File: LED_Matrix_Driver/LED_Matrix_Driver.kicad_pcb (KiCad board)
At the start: 4 copper layers, 76 parts, among them J1 Audio In, J2 Screw_Terminal_01x02, J3 Buttons, J4 LED Anode Rows, J5 Columns 24-31 LED Cathodes, J6 Columns 16-23 LED Cathodes, J7 Columns 8-15 LED Cathodes, J8 Columns 0-7 LED Cathodes, U1 ESP32-DEVKITC-32E, U2 74HCT244, U3 MIC2981, U4 74HC238, U5 HEF4794B, U6 HEF4794B, U7 HEF4794B, U8 HEF4794B

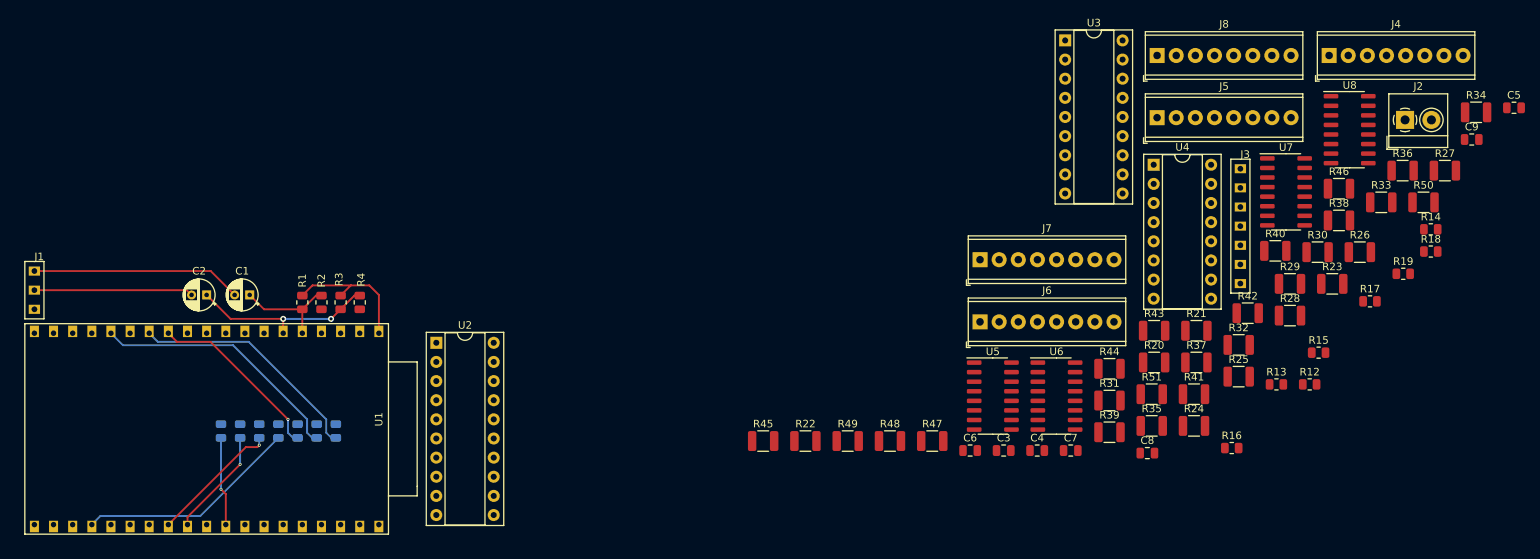
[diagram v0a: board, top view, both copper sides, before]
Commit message: Finished PCB design for board revision 1.1
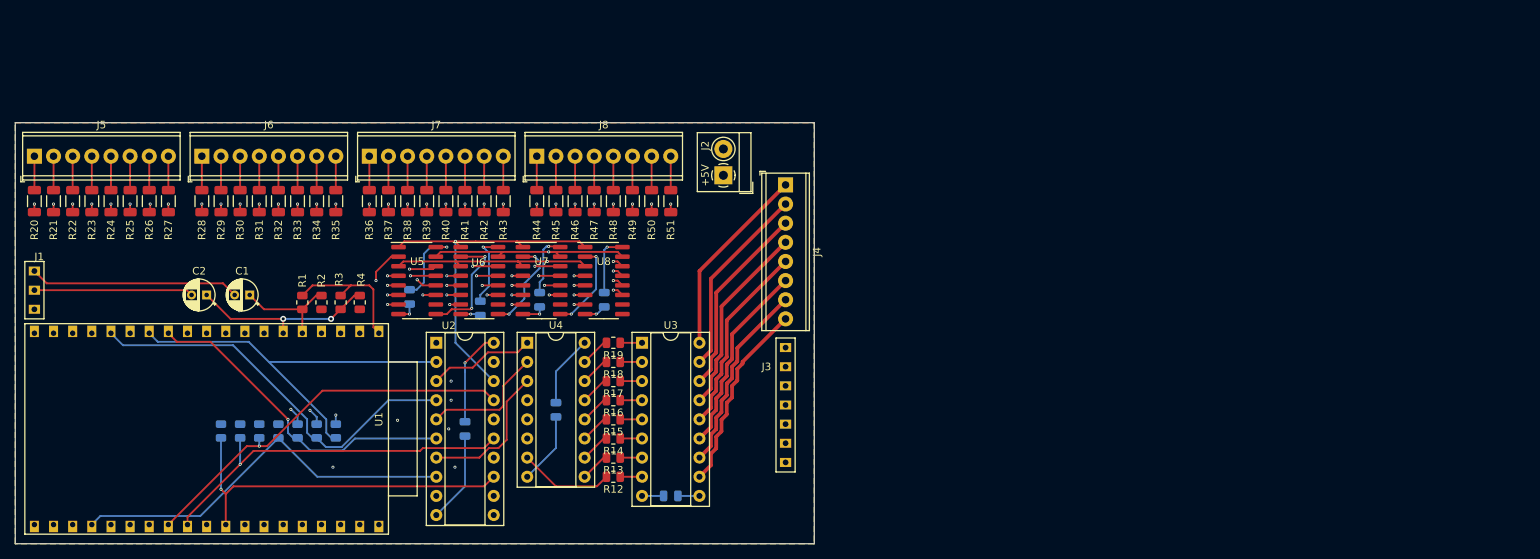
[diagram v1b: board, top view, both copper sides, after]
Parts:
- C3, C4, C5, C6, C7, C8, C9: moved to B.Cu
- R20, R21, R22, R23, R24, R25, R26, R27, R28, R29, R30, R31, R32, R33, R34, R35, R36, R37, R38, R39, R40, R41, R42, R43, R44, R45, R46, R47, R48, R49, R50, R51: footprint Resistor_SMD:R_1210_3225Metric -> Resistor_SMD:R_1206_3216Metric
- moved R27 169.5 mm to (32.4, 91.7), turned to 270 degrees
- moved R23 165.0 mm to (22.2, 91.7), turned to 270 degrees
- moved R26 160.8 mm to (29.8, 91.7), turned to 270 degrees
- moved R34 154.3 mm to (52.1, 91.7), turned to 270 degrees
- moved R21 152.7 mm to (17.1, 91.7), turned to 270 degrees
- moved R20 150.1 mm to (14.6, 91.7), turned to 270 degrees
- moved J5 149.1 mm to (14.6, 85.7)
- moved R25 149.0 mm to (27.3, 91.7), turned to 270 degrees
- moved R24 146.8 mm to (24.8, 91.7), turned to 270 degrees
- moved R28 145.2 mm to (36.8, 91.7), turned to 270 degrees
- moved R33 143.8 mm to (49.5, 91.7), turned to 270 degrees
- moved R30 143.2 mm to (41.9, 91.7), turned to 270 degrees
- moved R29 142.3 mm to (39.4, 91.7), turned to 270 degrees
- moved R36 137.2 mm to (59.1, 91.7), turned to 270 degrees
- moved C5 133.3 mm to (83.8, 119.4), turned to 270 degrees
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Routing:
- net Net-(J3-Pad6): track 0.00 -> 93.6 mm
- net Net-(J3-Pad5): track 0.00 -> 92.7 mm
- net Net-(J3-Pad1): track 0.00 -> 91.7 mm
- net Net-(J3-Pad2): track 0.00 -> 84.4 mm
- net Net-(J3-Pad3): track 0.00 -> 74.6 mm
- net Net-(J3-Pad4): track 0.00 -> 69.9 mm
- net Net-(U2-Pad12): track 0.00 -> 66.5 mm, vias 0 -> 1
- net +5V: track 0.00 -> 62.8 mm, vias 0 -> 5
- net Net-(U2-Pad14): track 0.00 -> 58.8 mm, vias 0 -> 1
- net Net-(R22-Pad2): track 0.00 -> 54.2 mm, vias 0 -> 2
- net Net-(R20-Pad2): track 0.00 -> 53.2 mm, vias 0 -> 2
- net Net-(R23-Pad2): track 0.00 -> 53.0 mm, vias 0 -> 2
- net Net-(R21-Pad2): track 0.00 -> 51.2 mm, vias 0 -> 2
- net Net-(U2-Pad18): track 0.00 -> 48.2 mm, vias 0 -> 1
- net Net-(R24-Pad2): track 0.00 -> 48.0 mm, vias 0 -> 2
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- added copper zone on In4.Cu, net +5V
- added copper zone on B.Cu, net Earth
- added copper zone on F.Cu, net Earth
- added copper zone on In1.Cu, net Earth
- added copper zone on In2.Cu, net Earth
- added copper zone on In3.Cu, net Earth
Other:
- board outline added: 106 x 55.9 mm
- copper layers 4 -> 6
- board text added: "+5V"
